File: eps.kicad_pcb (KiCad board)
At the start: 4 copper layers, 95.9 x 90.2 mm, 141 parts, among them J1 CONN_01X05, J2 CONN_01X05, J3 CONN_01X05, J4 CONN_01X05, J5 +BATT, J6 -BATT, J7 PROGRAMMING PORT, J8 H_EPS, J9 DEBUG, Q1 BSC026NE2LS5, Q2 BSC026NE2LS5, Q3 BSC026NE2LS5, Q4 BSC026NE2LS5, Q5 BSC026NE2LS5, Q6 BSC026NE2LS5, SW1 SW_RST, U1 ATMEGA32M1-MU, U10 ADS7952, U11 TPS630250, U12 bq297xx, U13 INA214, U14 INA214, U15 TPS630250, U16 TPS61088, U17 TPS61088, U18 ADS7952, U19 INA214, U2 INA214, U20 INA214, U21 INA214, U22 REF5025, U23 REF5025, U3 INA214, U4 INA214, U5 INA214, U6 ADA4891-4, U7 ADA4891-4, U8 SN65HVD230, U9 SST25VF016B, Y1 8MHz

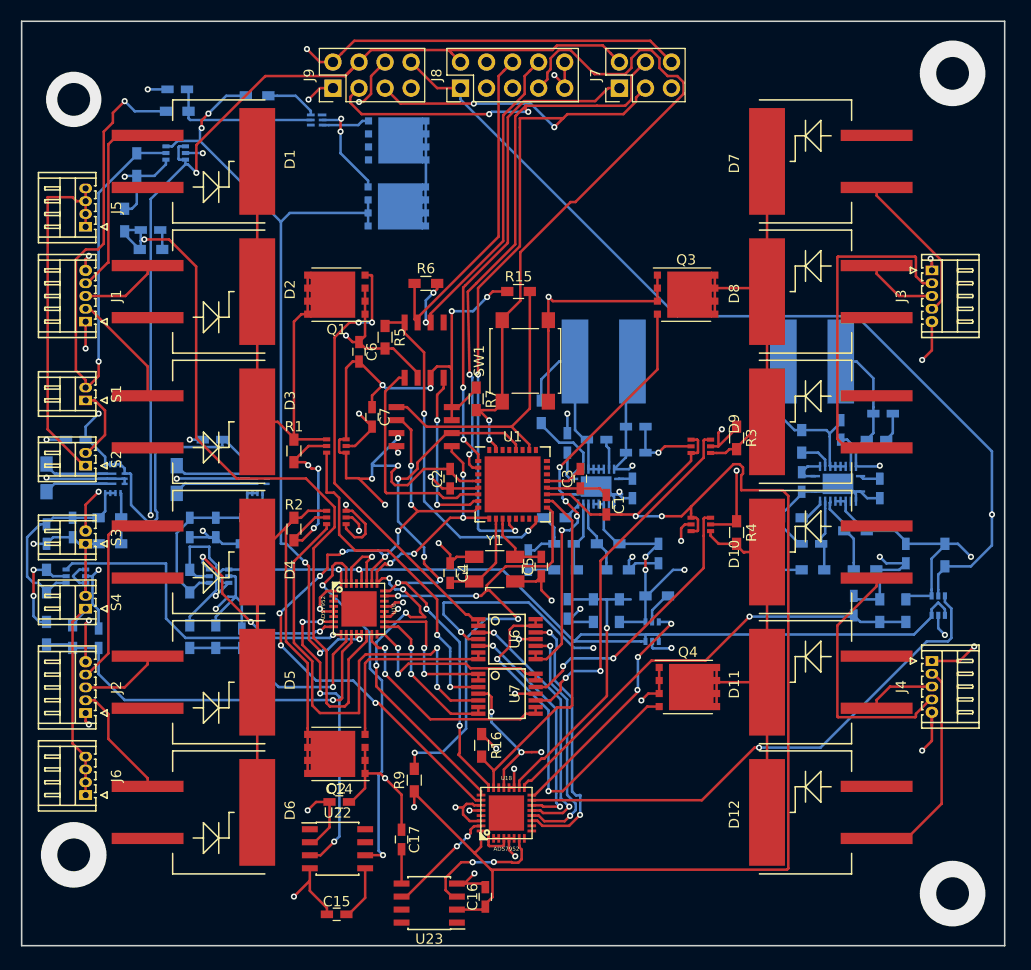
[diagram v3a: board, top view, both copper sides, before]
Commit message: Resized pads
J2, J3, J4, S4
X = 1.1 mm
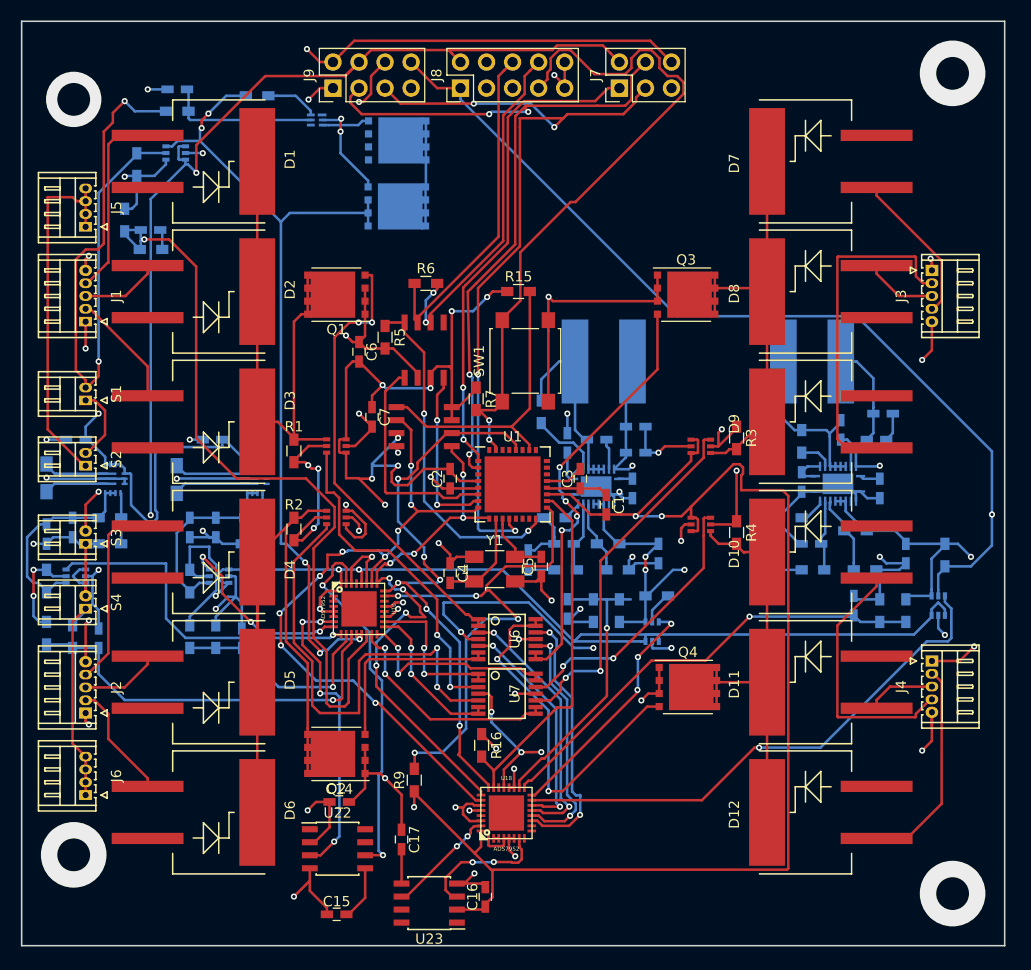
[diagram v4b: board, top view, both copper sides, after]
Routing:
- net (no net): track 0.00 -> 6.66 mm, vias 0 -> 4
- net GND: track 341.7 -> 335.0 mm, vias 63 -> 59
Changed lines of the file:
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@@
-(kicad_pcb (version 4) (host pcbnew 4.0.6)
+(kicad_pcb (version 4) (host pcbnew 4.0.7)
   (general
     (links 467)
@@
     (2 GND power)
     (31 B.Cu signal)
-    (32 B.Adhes user hide)
-    (33 F.Adhes user hide)
-    (34 B.Paste user hide)
-    (35 F.Paste user hide)
-    (36 B.SilkS user hide)
-    (37 F.SilkS user hide)
-    (38 B.Mask user hide)
-    (39 F.Mask user hide)
-    (40 Dwgs.User user hide)
-    (41 Cmts.User user hide)
-    (42 Eco1.User user hide)
-    (43 Eco2.User user hide)
+    (32 B.Adhes user)
+    (33 F.Adhes user)
+    (34 B.Paste user)
+    (35 F.Paste user)
+    (36 B.SilkS user)
+    (37 F.SilkS user)
+    (38 B.Mask user)
+    (39 F.Mask user)
+    (40 Dwgs.User user)
+    (41 Cmts.User user)
+    (42 Eco1.User user)
+    (43 Eco2.User user)
     (44 Edge.Cuts user)
-    (45 Margin user hide)
-    (46 B.CrtYd user hide)
-    (47 F.CrtYd user hide)
-    (48 B.Fab user hide)
-    (49 F.Fab user hide)
+    (45 Margin user)
+    (46 B.CrtYd user)
+    (47 F.CrtYd user)
+    (48 B.Fab user)
+    (49 F.Fab user)
   )
   (setup
@@
     (fp_line (start 7.05 1.5) (end 7.05 -5.1) (layer F.CrtYd) (width 0.05))
     (fp_line (start 7.05 -5.1) (end -2.05 -5.1) (layer F.CrtYd) (width 0.05))
-    (pad 1 thru_hole rect (at 0 0 90) (size 0.95 1.25) (drill 0.6) (layers *.Cu *.Mask)
+    (pad 1 thru_hole rect (at 0 0 90) (size 1.1 1.25) (drill 0.6) (layers *.Cu *.Mask)
       (net 1 GND))
     (pad 2 thru_hole oval (at 1.25 0 90) (size 0.95 1.25) (drill 0.6) (layers *.Cu *.Mask)
@@
     (fp_line (start 7.05 1.5) (end 7.05 -5.1) (layer F.CrtYd) (width 0.05))
     (fp_line (start 7.05 -5.1) (end -2.05 -5.1) (layer F.CrtYd) (width 0.05))
-    (pad 1 thru_hole rect (at 0 0 270) (size 0.95 1.25) (drill 0.6) (layers *.Cu *.Mask)
+    (pad 1 thru_hole rect (at 0 0 270) (size 1.1 1.25) (drill 0.6) (layers *.Cu *.Mask)
       (net 1 GND))
     (pad 2 thru_hole oval (at 1.25 0 270) (size 0.95 1.25) (drill 0.6) (layers *.Cu *.Mask)
@@
     (fp_line (start 7.05 1.5) (end 7.05 -5.1) (layer F.CrtYd) (width 0.05))
     (fp_line (start 7.05 -5.1) (end -2.05 -5.1) (layer F.CrtYd) (width 0.05))
-    (pad 1 thru_hole rect (at 0 0 270) (size 0.95 1.25) (drill 0.6) (layers *.Cu *.Mask)
+    (pad 1 thru_hole rect (at 0 0 270) (size 1.1 1.25) (drill 0.6) (layers *.Cu *.Mask)
       (net 1 GND))
     (pad 2 thru_hole oval (at 1.25 0 270) (size 0.95 1.25) (drill 0.6) (layers *.Cu *.Mask)
@@
     (pad 1 thru_hole rect (at 0 0 90) (size 0.95 1.25) (drill 0.6) (layers *.Cu *.Mask)
       (net 137 "Net-(J6-Pad1)"))
-    (pad 2 thru_hole oval (at 1.25 0 90) (size 0.95 1.25) (drill 0.6) (layers *.Cu *.Mask)
+    (pad 2 thru_hole oval (at 1.25 0 90) (size 1.1 1.25) (drill 0.6) (layers *.Cu *.Mask)
       (net 140 "Net-(S3-Pad1)"))
     (model ${KISYS3DMOD}/Connectors_Hirose.3dshapes/Hirose_DF13-02P-1.25DS_02x1.25mm_Angled.wrl
@@
   (gr_line (start 196 49.83) (end 100.11 49.83) (angle 90) (layer Edge.Cuts) (width 0.15))
   (gr_line (start 196 49.83) (end 196 140) (angle 90) (layer Edge.Cuts) (width 0.15))
-  (segment (start 105.16 131.11) (end 104.98 131.11) (width 0.25) (layer B.Cu) (net 1))
-  (segment (start 105.19 131.14) (end 105.16 131.11) (width 0.25) (layer B.Cu) (net 1))
-  (via (at 105.19 131.14) (size 6.4) (drill 3.2) (layers F.Cu B.Cu) (net 1))
-  (via (at 105.19 57.45) (size 5.4) (drill 3.2) (layers F.Cu B.Cu) (net 1))
+  (segment (start 105.16 131.11) (end 104.98 131.11) (width 0.25) (layer B.Cu) (net 0))
+  (segment (start 105.19 131.14) (end 105.16 131.11) (width 0.25) (layer B.Cu) (net 0))
+  (via (at 105.19 131.14) (size 6.4) (drill 3.2) (layers F.Cu B.Cu) (net 0))
+  (via (at 105.19 57.45) (size 5.4) (drill 3.2) (layers F.Cu B.Cu) (net 0))
+  (segment (start 190.41 55.42) (end 190.92 54.91) (width 0.25) (layer GND) (net 0))
+  (segment (start 190.41 55.42) (end 190.92 54.91) (width 0.25) (layer GND) (net 0))
+  (segment (start 188.9 56.93) (end 190.41 55.42) (width 0.25) (layer GND) (net 0))
+  (via (at 190.92 54.91) (size 6.4) (drill 3.2) (layers F.Cu B.Cu) (net 0))
+  (segment (start 188.9 132.9) (end 190.92 134.92) (width 0.25) (layer GND) (net 0))
+  (via (at 190.92 134.92) (size 6.4) (drill 3.2) (layers F.Cu B.Cu) (net 0))
   (via (at 112.41 56.47) (size 0.6) (drill 0.3) (layers F.Cu B.Cu) (net 1))
   (segment (start 112.41 56.47) (end 114.34 56.47) (width 0.25) (layer B.Cu) (net 1))
-  (segment (start 190.41 55.42) (end 190.92 54.91) (width 0.25) (layer GND) (net 1))
-  (segment (start 190.41 55.42) (end 190.92 54.91) (width 0.25) (layer GND) (net 1))
-  (segment (start 188.9 56.93) (end 190.41 55.42) (width 0.25) (layer GND) (net 1))
-  (via (at 190.92 54.91) (size 6.4) (drill 3.2) (layers F.Cu B.Cu) (net 1))
-  (segment (start 188.9 132.9) (end 190.92 134.92) (width 0.25) (layer GND) (net 1))
-  (via (at 190.92 134.92) (size 6.4) (drill 3.2) (layers F.Cu B.Cu) (net 1))
   (segment (start 188.9 74.13) (end 188.9 73.405) (width 0.25) (layer F.Cu) (net 1))
   (segment (start 106.35 112.31) (end 106.35 108.59) (width 0.25) (layer F.Cu) (net 1))
